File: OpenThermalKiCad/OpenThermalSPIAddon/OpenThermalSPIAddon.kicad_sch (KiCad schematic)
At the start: 3 parts

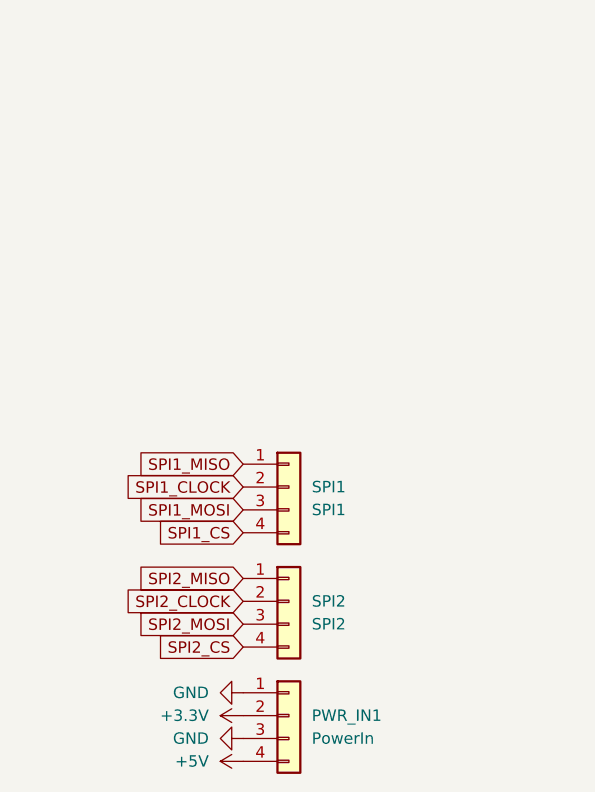
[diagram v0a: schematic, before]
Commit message: Updated wiring + components
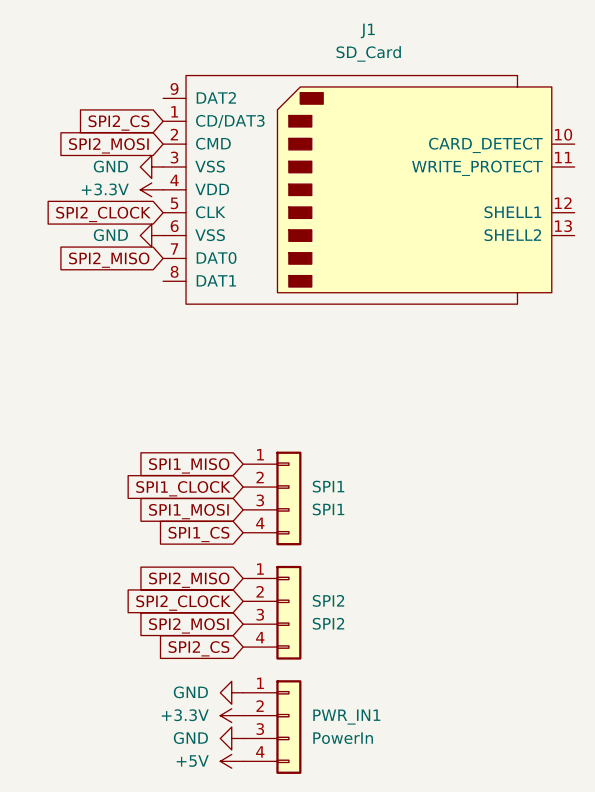
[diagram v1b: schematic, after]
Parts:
- added J1: SD_Card, Connector_Card:SD_Kyocera_145638009211859+, symbol Connector:SD_Card
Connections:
- net +3.3V: now also J1.4 (VDD)
- net GND: now also J1.3 (VSS), J1.6 (VSS)
- net SPI2_CLOCK: now also J1.5 (CLK)
- net SPI2_CS: now also J1.1 (CD/DAT3)
- net SPI2_MISO: now also J1.7 (DAT0)
- net SPI2_MOSI: now also J1.2 (CMD)
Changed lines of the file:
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@@
+    )
+  )
+  (global_label "SPI2_MOSI" (shape input) (at 105.41 41.91 180) (fields_autoplaced)
+    (effects (font (size 1.27 1.27)) (justify right))
+    (property "Intersheetrefs" "${INTERSHEET_REFS}" (at 92.5672 41.91 0)
+      (effects (font (size 1.27 1.27)) (justify right) hide)
     )
   )
@@
     )
   )
+  (global_label "SPI2_MISO" (shape input) (at 105.41 54.61 180) (fields_autoplaced)
+    (effects (font (size 1.27 1.27)) (justify right))
+    (property "Intersheetrefs" "${INTERSHEET_REFS}" (at 92.5672 54.61 0)
+      (effects (font (size 1.27 1.27)) (justify right) hide)
+    )
+  )
   (global_label "SPI1_MISO" (shape input) (at 114.3 77.47 180) (fields_autoplaced)
     (effects (font (size 1.27 1.27)) (justify right))
@@
     )
   )
+  (global_label "SPI2_CLOCK" (shape input) (at 105.41 49.53 180) (fields_autoplaced)
+    (effects (font (size 1.27 1.27)) (justify right))
+    (property "Intersheetrefs" "${INTERSHEET_REFS}" (at 90.9948 49.53 0)
+      (effects (font (size 1.27 1.27)) (justify right) hide)
+    )
+  )
+  (global_label "SPI2_CS" (shape input) (at 105.41 39.37 180) (fields_autoplaced)
+    (effects (font (size 1.27 1.27)) (justify right))
+    (property "Intersheetrefs" "${INTERSHEET_REFS}" (at 94.6839 39.37 0)
+      (effects (font (size 1.27 1.27)) (justify right) hide)
+    )
+  )
   (global_label "SPI2_CLOCK" (shape input) (at 114.3 92.71 180) (fields_autoplaced)
     (effects (font (size 1.27 1.27)) (justify right))
@@
     (property "Intersheetrefs" "${INTERSHEET_REFS}" (at 103.5739 85.09 0)
       (effects (font (size 1.27 1.27)) (justify right) hide)
+    )
+  )
+  (symbol (lib_id "power:GND") (at 105.41 52.07 270) (unit 1)
+    (in_bom yes) (on_board yes) (dnp no) (fields_autoplaced)
+    (property "Reference" "#PWR03" (at 99.06 52.07 0)
+      (effects (font (size 1.27 1.27)) hide)
+    )
+    (property "Value" "GND" (at 101.6 52.07 90)
+      (effects (font (size 1.27 1.27)) (justify right))
+    )
+    (property "Footprint" "" (at 105.41 52.07 0)
+      (effects (font (size 1.27 1.27)) hide)
+    )
+    (property "Datasheet" "" (at 105.41 52.07 0)
+      (effects (font (size 1.27 1.27)) hide)
+    )
+    (pin "1")
+    (instances
+      (project "OpenThermalSPIAddon"
+        (path "/021bc0b3-a3b3-409b-b422-0b07c088ccb6"
+          (reference "#PWR03") (unit 1)
+        )
+      )
     )
   )
@@
     )
   )
+  (symbol (lib_id "power:GND") (at 105.41 44.45 270) (unit 1)
+    (in_bom yes) (on_board yes) (dnp no) (fields_autoplaced)
+    (property "Reference" "#PWR02" (at 99.06 44.45 0)
+      (effects (font (size 1.27 1.27)) hide)
+    )
+    (property "Value" "GND" (at 101.6 44.45 90)
+      (effects (font (size 1.27 1.27)) (justify right))
+    )
+    (property "Footprint" "" (at 105.41 44.45 0)
+      (effects (font (size 1.27 1.27)) hide)
+    )
+    (property "Datasheet" "" (at 105.41 44.45 0)
+      (effects (font (size 1.27 1.27)) hide)
+    )
+    (pin "1")
+    (instances
+      (project "OpenThermalSPIAddon"
+        (path "/021bc0b3-a3b3-409b-b422-0b07c088ccb6"
+          (reference "#PWR02") (unit 1)
+        )
+      )
+    )
+  )
   (symbol (lib_id "Connector_Generic:Conn_01x04") (at 119.38 105.41 0) (unit 1)
     (in_bom yes) (on_board yes) (dnp no) (fields_autoplaced)
@@
         )
       )
+    )
+  )
+  (symbol (lib_id "Connector:SD_Card") (at 128.27 46.99 0) (unit 1)
+    (in_bom yes) (on_board yes) (dnp no) (fields_autoplaced)
+    (property "Reference" "J1" (at 128.27 29.21 0)
+      (effects (font (size 1.27 1.27)))
+    )
+    (property "Value" "SD_Card" (at 128.27 31.75 0)
+      (effects (font (size 1.27 1.27)))
+    )
+    (property "Footprint" "Connector_Card:SD_Kyocera_145638009211859+" (at 128.27 46.99 0)
+      (effects (font (size 1.27 1.27)) hide)
+    )
+    (property "Datasheet" "http://portal.fciconnect.com/Comergent//fci/drawing/10067847.pdf" (at 128.27 46.99 0)
+      (effects (font (size 1.27 1.27)) hide)
+    )
+    (pin "2")
+    (pin "11")
+    (pin "5")
+    (pin "8")
+    (pin "12")
+    (pin "10")
+    (pin "7")
+    (pin "9")
+    (pin "1")
+    (pin "13")
+    (pin "6")
+    (pin "3")
+    (pin "4")
+    (instances
+      (project "OpenThermalSPIAddon"
+        (path "/021bc0b3-a3b3-409b-b422-0b07c088ccb6"
+          (reference "J1") (unit 1)
+        )
+      )
+    )
+  )
+  (symbol (lib_id "power:+3.3V") (at 105.41 46.99 90) (unit 1)
+    (in_bom yes) (on_board yes) (dnp no) (fields_autoplaced)
+    (property "Reference" "#PWR01" (at 109.22 46.99 0)
+      (effects (font (size 1.27 1.27)) hide)
+    )
+    (property "Value" "+3.3V" (at 101.6 46.99 90)
+      (effects (font (size 1.27 1.27)) (justify left))
+    )
+    (property "Footprint" "" (at 105.41 46.99 0)
+      (effects (font (size 1.27 1.27)) hide)
+    )
+    (property "Datasheet" "" (at 105.41 46.99 0)
+      (effects (font (size 1.27 1.27)) hide)
+    )
+    (pin "1")
+    (instances
+      (project "OpenThermalSPIAddon"
+        (path "/021bc0b3-a3b3-409b-b422-0b07c088ccb6"
+          (reference "#PWR01") (unit 1)
+        )
+      )
